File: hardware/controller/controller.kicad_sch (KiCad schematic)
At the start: 63 parts, among them J1 USB-C, J10 BTB 40P header, J11 BTB 40P header, J2 Qwiic, J3 Qwiic, Q1 AO3401A, SW1 BTN1, SW2 BTN2, SW3 BOOTSEL, U1 RP2354B, U2 TPD2E2U06, U3 ME6211C33M5G, U4 74AHCT1G125, Y1 12MHz

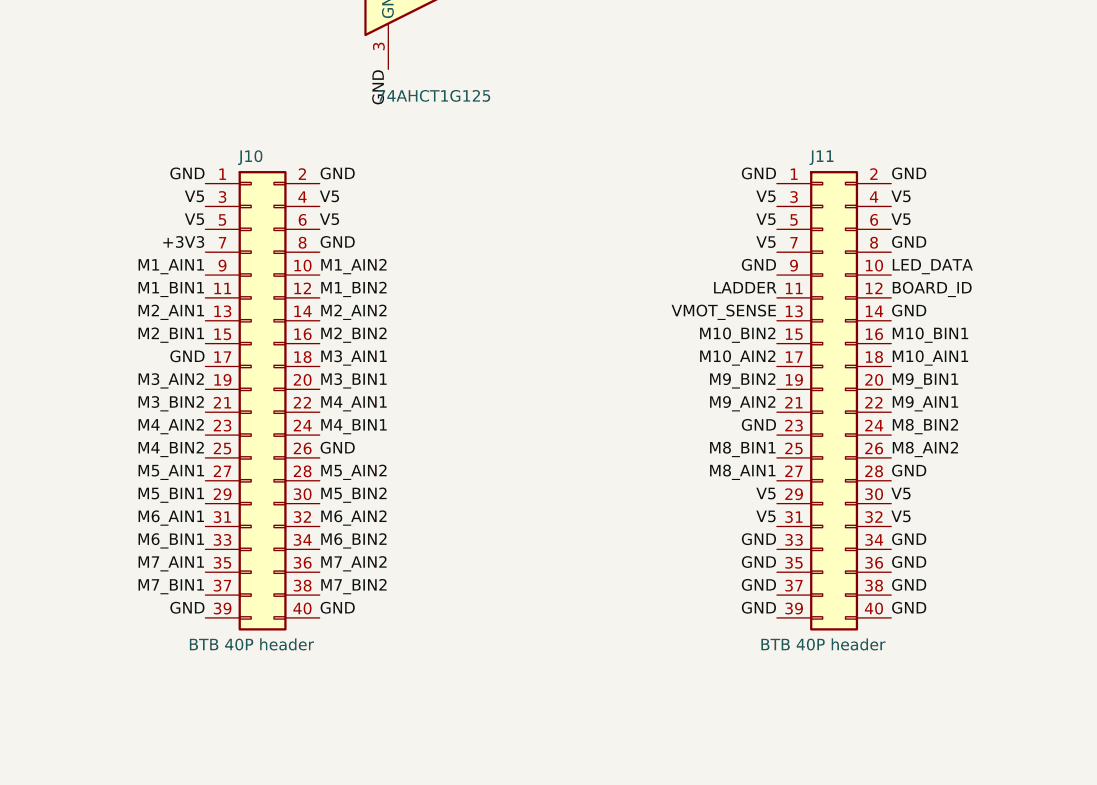
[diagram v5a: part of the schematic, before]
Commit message: Controller: fully routed
- BTN1/BTN2 -> XUNPU TS-1088-AR02016 (C720477), stacked in the top-right
  corner with R11/R12 under them: the TS-1187A pads over the BTB headers
  blocked the connector fan-out.
- Connector B moved 2 mm down (stack still keyed by A's +2 mm offset);
  ladder/board-ID resistor column moved right, out of the M8 path.
- BTB corner contacts left unconnected (Hirose metal fittings).
- Routing: Freerouting 2.5.0 for the bulk, then a small grid router for
  the remaining nets and plane stitching. DRC: 0 unconnected, only
  silkscreen warnings and one harmless track stub left.

Co-Authored-By: Claude Opus 5.5 <noreply@anthropic.com>
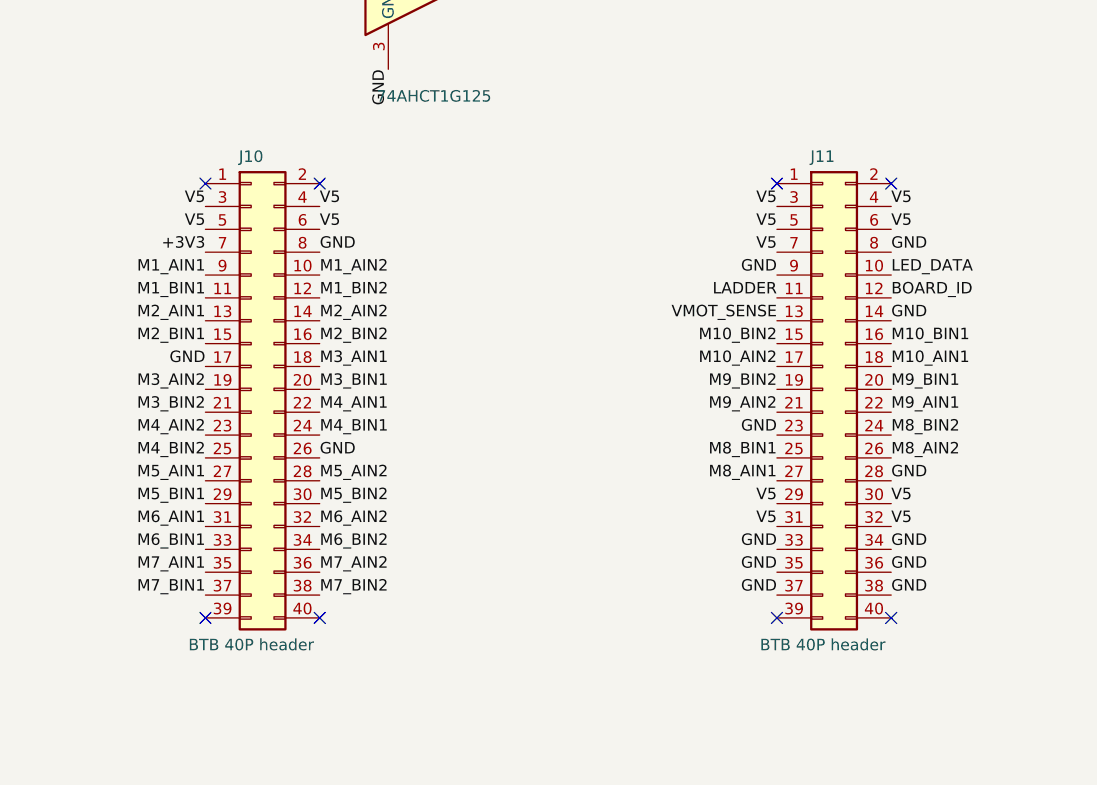
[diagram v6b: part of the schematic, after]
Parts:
- SW1, SW2: footprint Button_Switch_SMD:SW_Push_1P1T_XKB_TS-1187A -> Button_Switch_SMD:SW_SPST_TS-1088-xR020; LCSC C318884 -> C720477; MPN TS-1187A-B-A-B -> TS-1088-AR02016; Note (none) -> XUNPU 3.9x3.0 mm 2-pad; small so the BTB fan-out routes
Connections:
- net GND: no longer J10.1 (Pin_1), J10.2 (Pin_2), J10.39 (Pin_39), J10.40 (Pin_40), J11.1 (Pin_1), J11.2 (Pin_2), J11.39 (Pin_39), J11.40 (Pin_40)
- no-connect marks 10 -> 18
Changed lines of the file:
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@@
 			)
 		)
-		(property "Footprint" "Button_Switch_SMD:SW_Push_1P1T_XKB_TS-1187A"
+		(property "Footprint" "Button_Switch_SMD:SW_SPST_TS-1088-xR020"
 			(at 368.3 264.16 0)
 			(hide yes)
@@
 			)
 		)
-		(property "LCSC" "C318884"
+		(property "LCSC" "C720477"
 			(at 368.3 264.16 0)
 			(hide yes)
@@
 			)
 		)
-		(property "MPN" "TS-1187A-B-A-B"
+		(property "MPN" "TS-1088-AR02016"
+			(at 368.3 264.16 0)
+			(hide yes)
+			(effects
+				(font
+					(size 1.27 1.27)
+				)
+			)
+		)
+		(property "Note" "XUNPU 3.9x3.0 mm 2-pad; small so the BTB fan-out routes"
 			(at 368.3 264.16 0)
 			(hide yes)
@@
 			)
 		)
-		(property "Footprint" "Button_Switch_SMD:SW_Push_1P1T_XKB_TS-1187A"
+		(property "Footprint" "Button_Switch_SMD:SW_SPST_TS-1088-xR020"
 			(at 477.52 264.16 0)
 			(hide yes)
@@
 			)
 		)
-		(property "LCSC" "C318884"
+		(property "LCSC" "C720477"
 			(at 477.52 264.16 0)
 			(hide yes)
@@
 			)
 		)
-		(property "MPN" "TS-1187A-B-A-B"
+		(property "MPN" "TS-1088-AR02016"
+			(at 477.52 264.16 0)
+			(hide yes)
+			(effects
+				(font
+					(size 1.27 1.27)
+				)
+			)
+		)
+		(property "Note" "XUNPU 3.9x3.0 mm 2-pad; small so the BTB fan-out routes"
 			(at 477.52 264.16 0)
 			(hide yes)
@@
 		)
 	)
-	(label "GND"
-		(at 241.3 320.04 180)
-		(effects
-			(font
-				(size 1.27 1.27)
-			)
-			(justify right bottom)
-		)
-	)
-	(label "GND"
-		(at 254 320.04 0)
-		(effects
-			(font
-				(size 1.27 1.27)
-			)
-			(justify left bottom)
-		)
+	(no_connect
+		(at 241.3 320.04)
+	)
+	(no_connect
+		(at 254 320.04)
 	)
 	(label "V5"
@@
 		)
 	)
-	(label "GND"
-		(at 241.3 368.3 180)
-		(effects
-			(font
-				(size 1.27 1.27)
-			)
-			(justify right bottom)
-		)
-	)
-	(label "GND"
-		(at 254 368.3 0)
-		(effects
-			(font
-				(size 1.27 1.27)
-			)
-			(justify left bottom)
-		)
+	(no_connect
+		(at 241.3 368.3)
+	)
+	(no_connect
+		(at 254 368.3)
 	)
 	(symbol
@@
 		)
 	)
-	(label "GND"
-		(at 304.8 320.04 180)
-		(effects
-			(font
-				(size 1.27 1.27)
-			)
-			(justify right bottom)
-		)
-	)
-	(label "GND"
-		(at 317.5 320.04 0)
-		(effects
-			(font
-				(size 1.27 1.27)
-			)
-			(justify left bottom)
-		)
+	(no_connect
+		(at 304.8 320.04)
+	)
+	(no_connect
+		(at 317.5 320.04)
 	)
 	(label "V5"
@@
 		)
 	)
-	(label "GND"
-		(at 304.8 368.3 180)
-		(effects
-			(font
-				(size 1.27 1.27)
-			)
-			(justify right bottom)
-		)
-	)
-	(label "GND"
-		(at 317.5 368.3 0)
-		(effects
-			(font
-				(size 1.27 1.27)
-			)
-			(justify left bottom)
-		)
+	(no_connect
+		(at 304.8 368.3)
+	)
+	(no_connect
+		(at 317.5 368.3)
 	)
 	(symbol

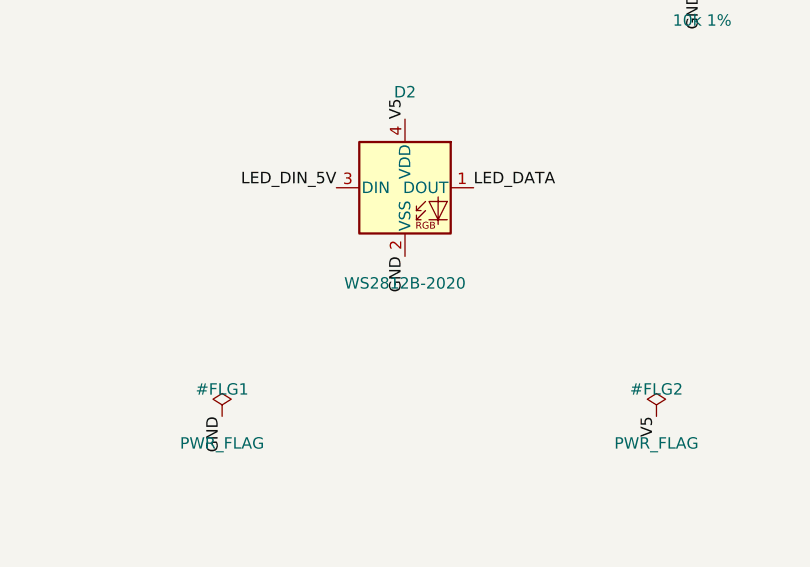
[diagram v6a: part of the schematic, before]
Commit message: single_sh: routed single-board PCB; BOM scrub
New single-board versions of the circuit (controller + driver + IO variant
on one PCB, BTBs removed): single_sh and single_xh schematics from single()
in gen/build.py. single_sh also gets a routed board:

- 122 x 20 mm, 4 layers, 1.6 mm, all parts on top. In1 GND; In2 V5 with a
  3V3 island under the MCU (thin finger to the LDO); F/B signals.
- Along the board: USB-C + power | drivers M4-M1 | MCU | drivers M10-M5 |
  LED strip. Motor connectors J12 J11 | J15 J14 J13 so each bus leaves the
  MCU in pin order; misc connectors along the other long edge.
- Driver cells pre-routed (A1/A2 cross B1/B2 on In2 jumpers), core
  regulator copied from the controller, rest Freerouting 2.5.0 + a small
  grid router. V5 via clusters at the FET, ext-5V diode and strip fuse.
- DRC: 0 errors, 0 unconnected, schematic parity clean; 24 silkscreen
  warnings (footprint outlines).
- gen/pcbgen.py: build() split out of main(), per-board size/thickness,
  polygon zones, single_sh() placement (reproduces the routed board).

BOOTSEL on the single boards is now the TS-1088-AR02016 (C720477), same as
BTN1/BTN2; the stacked controller keeps its TS-1187A.

BOM scrub (all boards; numbers checked against the JLCPCB library):
- Every passive gets LCSC/MPN (PASSIVES in gen/build.py), basic where one
  exists. VM caps now 16 V (basic 2.2 uF is 6.3 V).
- Polyfuse C702823 (not in JLCPCB's library) -> C209721, same rating.
- Status LED C965555 (1 in stock) -> XL-2020RGBC-WS2812B C5349955, same
  pinout and footprint.
- J8 B3B-PH-K-S gets C131339.
- Solder jumpers and test pads excluded from BOM and placement files
  (schgen in_bom support; pcbgen follows the symbol).
- Schematics and *_bom.csv regenerated; controller PCB fields/attributes
  synced (layout unchanged).

Co-Authored-By: Claude Opus 5.5 <noreply@anthropic.com>
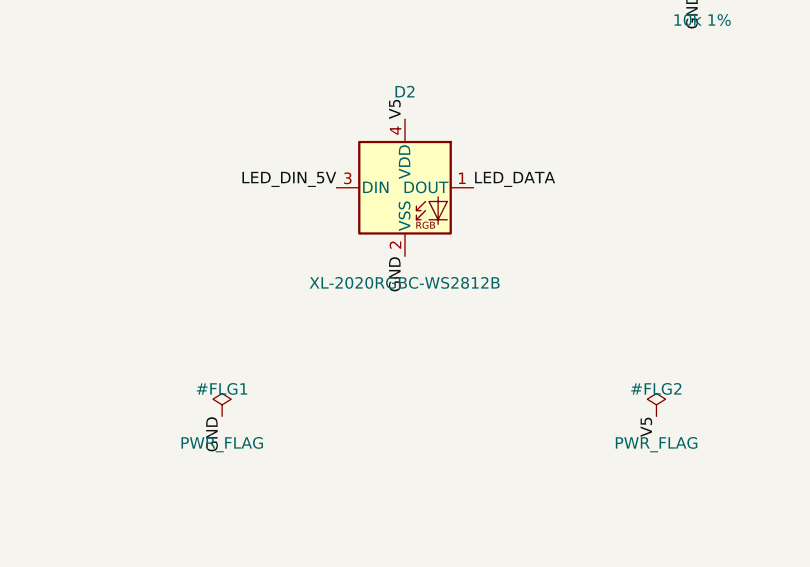
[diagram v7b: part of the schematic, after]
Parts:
- C1, C11, C12, C13, C2, C20, C22, C23, C24, C3, C4, C5, C6, C7, C8, C9: LCSC (none) -> C1525; MPN (none) -> CL05B104KO5NNNC
- C10, C14, C15: LCSC (none) -> C23733; MPN (none) -> CL05A475MP5NRNC
- C16, C17: LCSC (none) -> C1548; MPN (none) -> 0402CG150J500NT
- C18: LCSC (none) -> C15850; MPN (none) -> CL21A106KAYNNNE
- C19, C21: LCSC (none) -> C52923; MPN (none) -> CL05A105KA5NQNC
- D2: value WS2812B-2020 -> XL-2020RGBC-WS2812B; LCSC C965555 -> C5349955; MPN WS2812B-2020 -> XL-2020RGBC-WS2812B; Note (none) -> XINGLIGHT; WS2812B-2020 pinout and footprint; Worldsemi C96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
- F1: LCSC C702823 -> C209721; MPN SMD1812P150TF -> SMD1812P150TF/8; Note choose low resistance; alt C21002 -> PTTC; 1.5 A hold / 3 A trip, 8 V; alt C21002
- JP1, JP2, TP1, TP2, TP3, TP4, TP5: now left out of the parts list
- R1: LCSC (none) -> C25105; MPN (none) -> 0402WGF330JTCE
- R10, R11, R14: LCSC (none) -> C25744; MPN (none) -> 0402WGF1002TCE
- R12: LCSC (none) -> C25890; MPN (none) -> 0402WGF3301TCE
- R13, R2: LCSC (none) -> C11702; MPN (none) -> 0402WGF1001TCE
- R3, R4: LCSC (none) -> C25100; MPN (none) -> 0402WGF270JTCE
- R5, R6: LCSC (none) -> C25905; MPN (none) -> 0402WGF5101TCE
- R7: LCSC (none) -> C25741; MPN (none) -> 0402WGF1003TCE
- R8, R9: LCSC (none) -> C25900; MPN (none) -> 0402WGF4701TCE
